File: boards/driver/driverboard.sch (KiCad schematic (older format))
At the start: 39 parts, among them J1 RJ45, J2 RJ45, P1 HE10-10, Q1 NDS355, Q2 NDS355, Q3 NDS355, Q4 NDS355, Q5 NDS355, Q6 NDS355, Q7 NDS355, Q8 NDS355, U1 74HC595, U2 TS2937

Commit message: Small update on driverboard
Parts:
- R10, R3, R4, R5, R6, R7, R8, R9: value 200 -> 220
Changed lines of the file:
@@
 Sheet 1 1
 Title ""
-Date "26 jan 2014"
+Date "15 apr 2014"
 Rev ""
 Comp ""
@@
 P 8950 6600
 F 0 "R10" V 9030 6600 40  0000 C CNN
-F 1 "200" V 8957 6601 40  0000 C CNN
+F 1 "220" V 8957 6601 40  0000 C CNN
 F 2 "~" V 8880 6600 30  0000 C CNN
 F 3 "~" H 8950 6600 30  0000 C CNN
@@
 P 8950 5850
 F 0 "R9" V 9030 5850 40  0000 C CNN
-F 1 "200" V 8957 5851 40  0000 C CNN
+F 1 "220" V 8957 5851 40  0000 C CNN
 F 2 "~" V 8880 5850 30  0000 C CNN
 F 3 "~" H 8950 5850 30  0000 C CNN
@@
 P 8950 5100
 F 0 "R8" V 9030 5100 40  0000 C CNN
-F 1 "200" V 8957 5101 40  0000 C CNN
+F 1 "220" V 8957 5101 40  0000 C CNN
 F 2 "~" V 8880 5100 30  0000 C CNN
 F 3 "~" H 8950 5100 30  0000 C CNN
@@
 P 8950 4350
 F 0 "R7" V 9030 4350 40  0000 C CNN
-F 1 "200" V 8957 4351 40  0000 C CNN
+F 1 "220" V 8957 4351 40  0000 C CNN
 F 2 "~" V 8880 4350 30  0000 C CNN
 F 3 "~" H 8950 4350 30  0000 C CNN
@@
 P 8950 3600
 F 0 "R6" V 9030 3600 40  0000 C CNN
-F 1 "200" V 8957 3601 40  0000 C CNN
+F 1 "220" V 8957 3601 40  0000 C CNN
 F 2 "~" V 8880 3600 30  0000 C CNN
 F 3 "~" H 8950 3600 30  0000 C CNN
@@
 P 8950 2850
 F 0 "R5" V 9030 2850 40  0000 C CNN
-F 1 "200" V 8957 2851 40  0000 C CNN
+F 1 "220" V 8957 2851 40  0000 C CNN
 F 2 "~" V 8880 2850 30  0000 C CNN
 F 3 "~" H 8950 2850 30  0000 C CNN
@@
 P 8950 2100
 F 0 "R4" V 9030 2100 40  0000 C CNN
-F 1 "200" V 8957 2101 40  0000 C CNN
+F 1 "220" V 8957 2101 40  0000 C CNN
 F 2 "~" V 8880 2100 30  0000 C CNN
 F 3 "~" H 8950 2100 30  0000 C CNN
@@
 P 8950 1350
 F 0 "R3" V 9030 1350 40  0000 C CNN
-F 1 "200" V 8957 1351 40  0000 C CNN
+F 1 "220" V 8957 1351 40  0000 C CNN
 F 2 "~" V 8880 1350 30  0000 C CNN
 F 3 "~" H 8950 1350 30  0000 C CNN

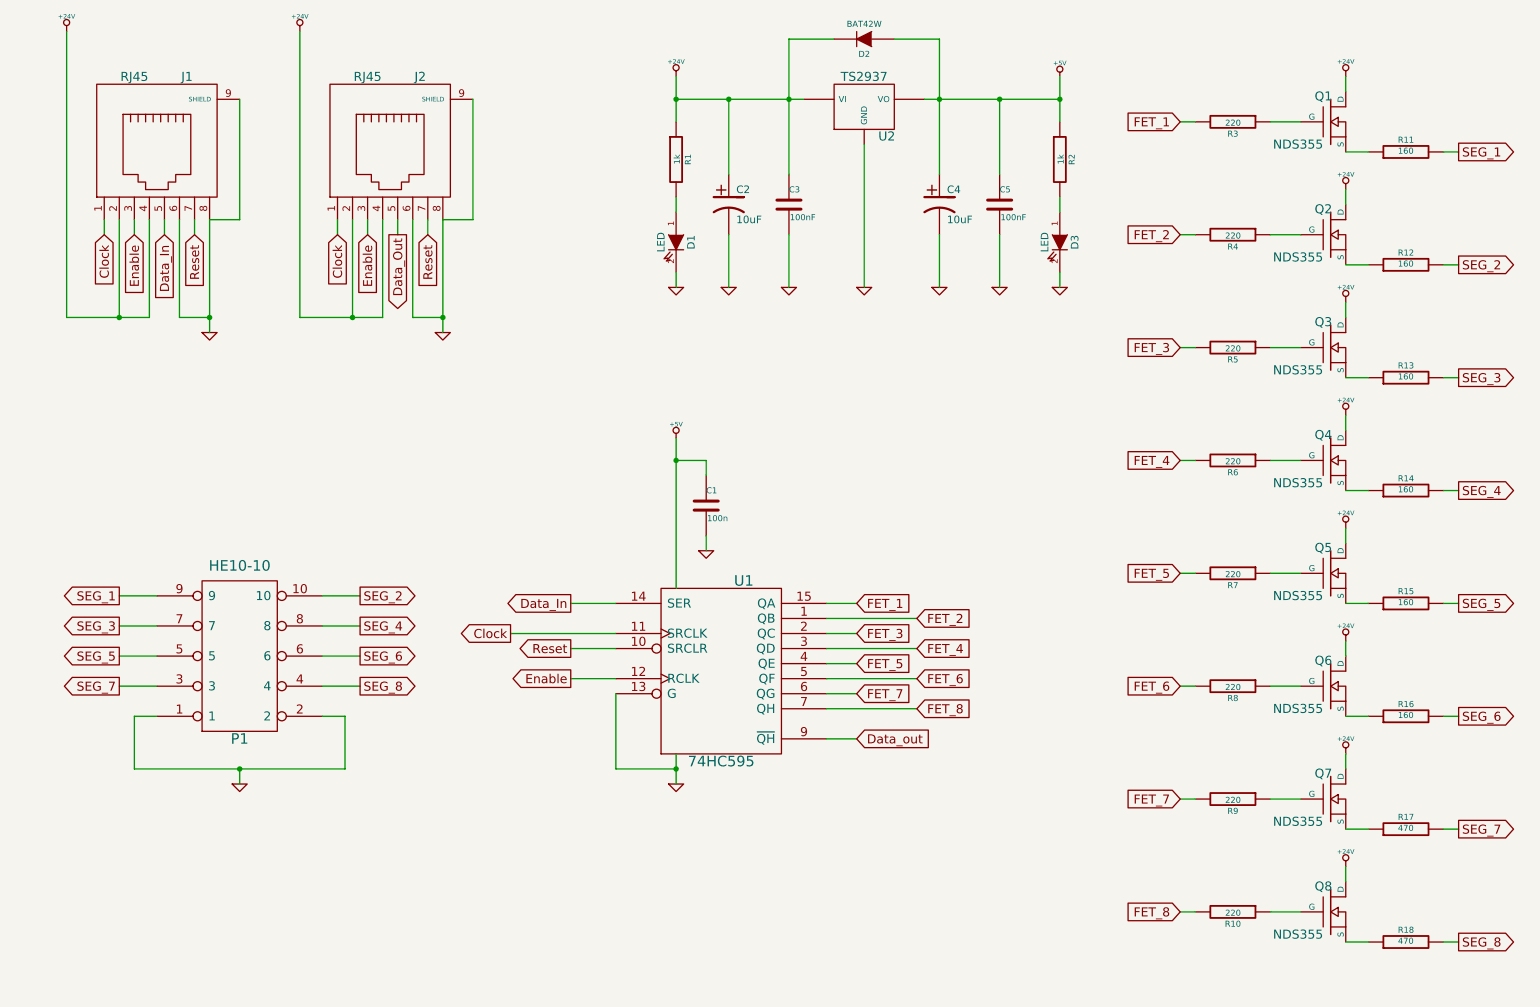
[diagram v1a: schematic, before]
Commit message: Started fixing schematics
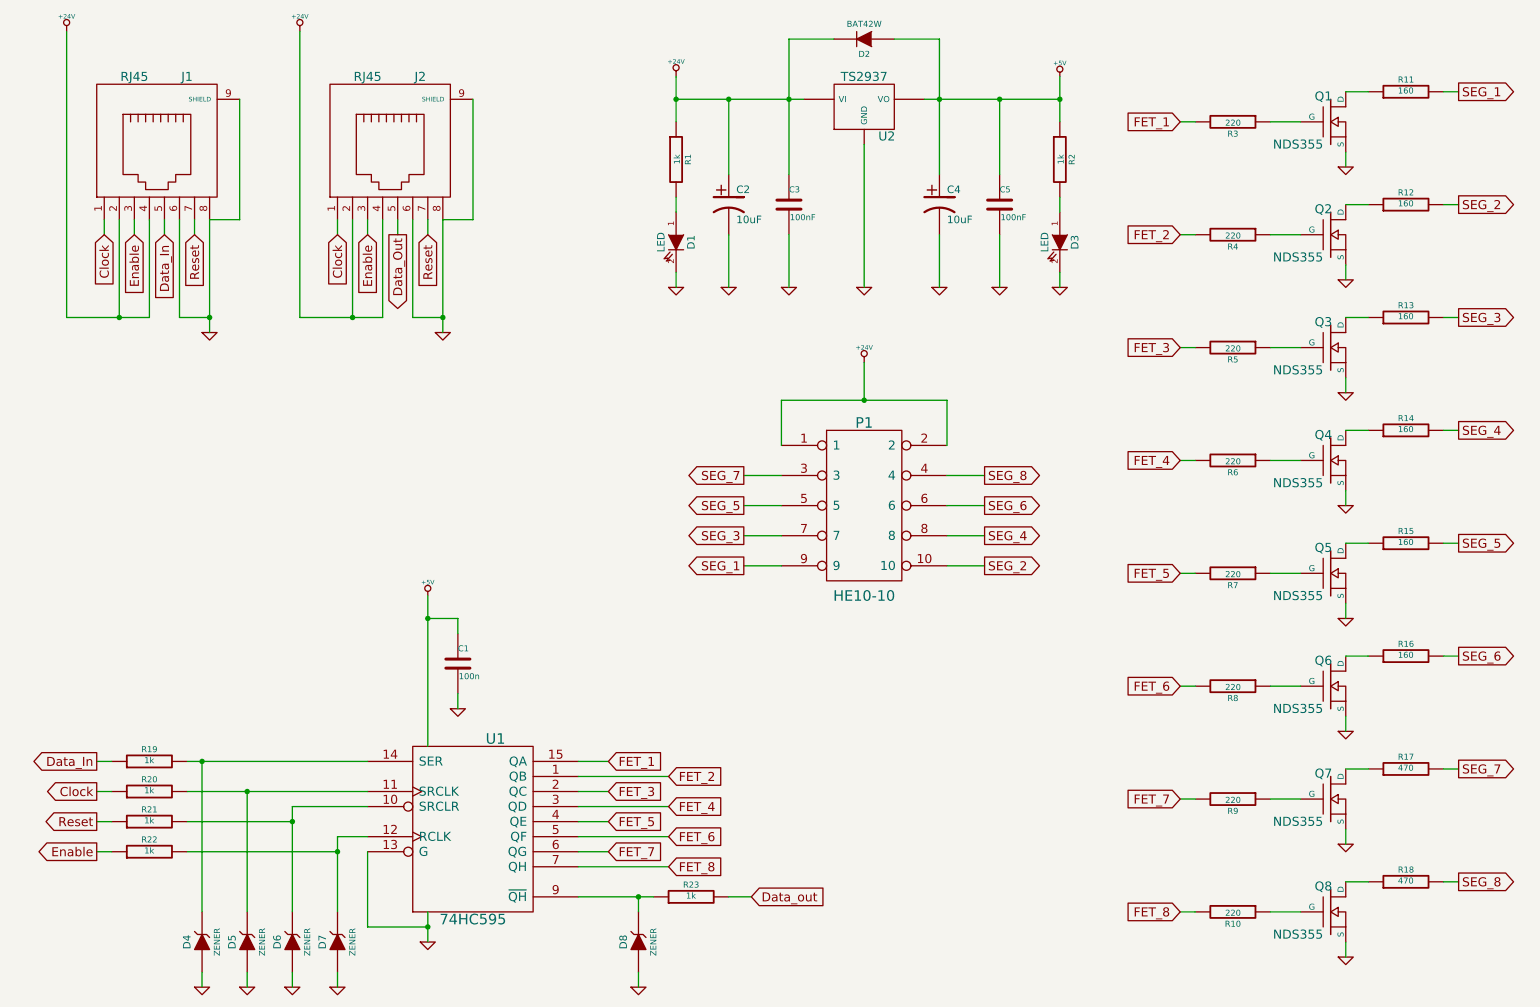
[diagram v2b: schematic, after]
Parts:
- added D4, D5, D6, D7, D8: ZENER, ~, symbol ZENER
- added R19, R20, R21, R22, R23: 1k, ~, symbol R
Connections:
- net +24V: now also P1.1, P1.2; no longer Q1.2 (D), Q2.2 (D), Q3.2 (D), Q4.2 (D), Q5.2 (D), Q6.2 (D), Q7.2 (D), Q8.2 (D)
- net Clock: now also R20.1; no longer U1.11 (SRCLK)
- net Data_In: now also R19.1; no longer U1.14 (SER)
- net Data_out: now also R23.2; no longer U1.9 (~QH)
- net Enable: now also R22.1; no longer U1.12 (RCLK)
- net GND: now also Q1.3 (S), Q2.3 (S), Q3.3 (S), Q4.3 (S), Q5.3 (S), Q6.3 (S), Q7.3 (S), Q8.3 (S), D4.1 (A), D5.1 (A), D6.1 (A), D7.1 (A), D8.1 (A); no longer P1.1, P1.2
- net Reset: now also R21.1; no longer U1.10 (SRCLR)
- net at R18.1: now also Q8.2 (D); no longer Q8.3 (S)
- net at R17.1: now also Q7.2 (D); no longer Q7.3 (S)
- net at R16.1: now also Q6.2 (D); no longer Q6.3 (S)
- net at R15.1: now also Q5.2 (D); no longer Q5.3 (S)
- net at R14.1: now also Q4.2 (D); no longer Q4.3 (S)
- net at R13.1: now also Q3.2 (D); no longer Q3.3 (S)
- net at R12.1: now also Q2.2 (D); no longer Q2.3 (S)
- net at R11.1: now also Q1.2 (D); no longer Q1.3 (S)
- new net: D6.2 (K), R21.2, U1.10 (SRCLR)
- new net: D5.2 (K), R20.2, U1.11 (SRCLK)
- new net: D7.2 (K), R22.2, U1.12 (RCLK)
- new net: D4.2 (K), R19.2, U1.14 (SER)
- new net: D8.2 (K), R23.1, U1.9 (~QH)
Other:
- moved on the sheet: C1, P1, R11, R12, R13, R14, R15, R16, R17, R18, U1

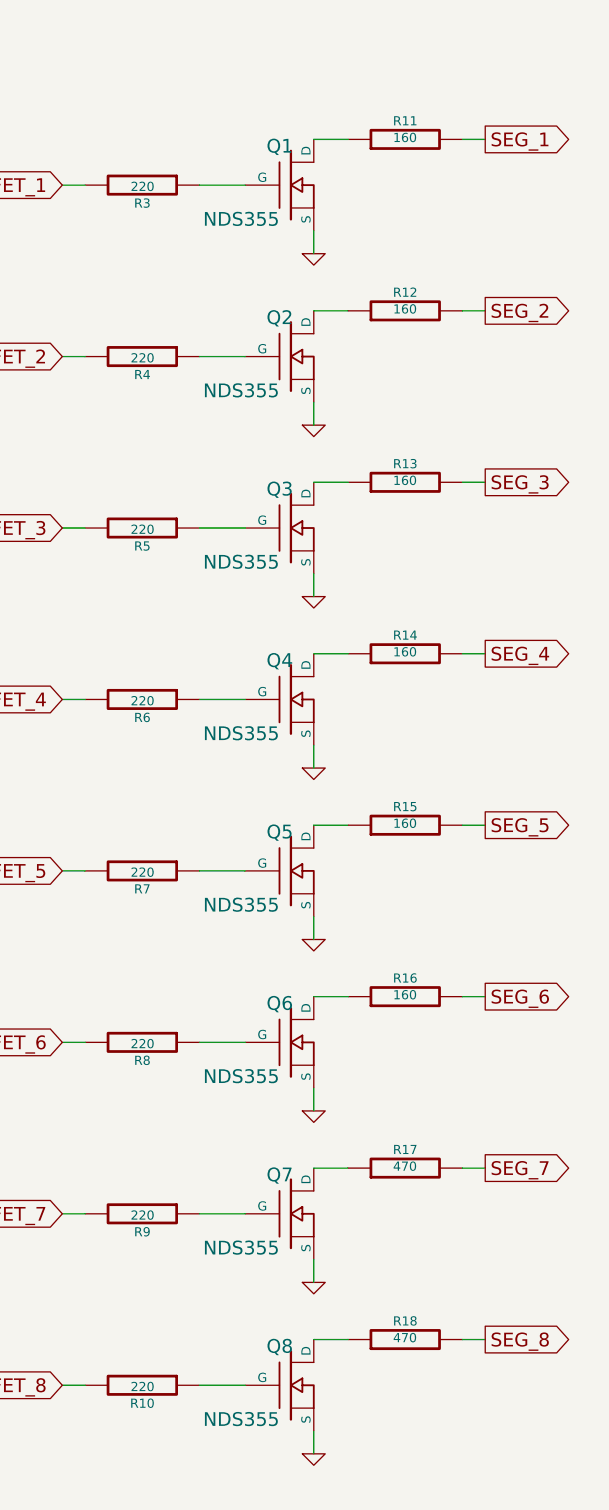
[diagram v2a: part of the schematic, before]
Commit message: Updated resistor values
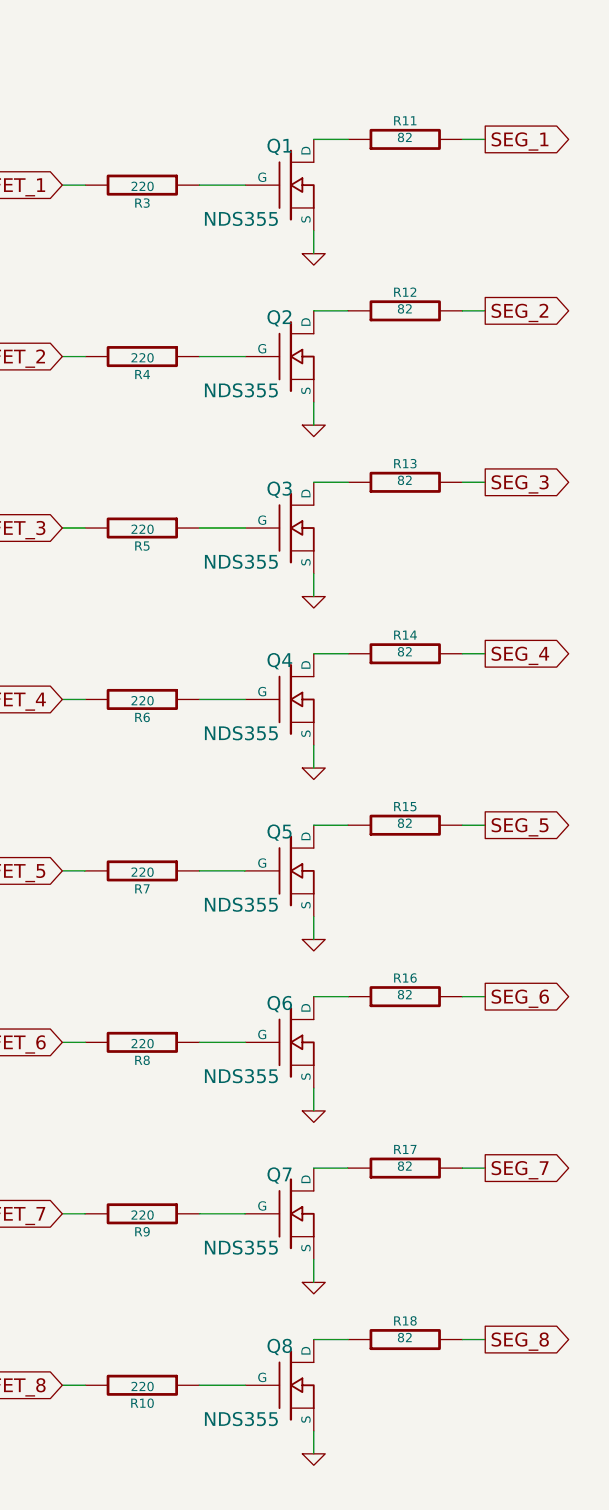
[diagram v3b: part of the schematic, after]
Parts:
- R11, R12, R13, R14, R15, R16: value 160 -> 82
- R17, R18: value 470 -> 82
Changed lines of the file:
@@
 Sheet 1 1
 Title ""
-Date "15 aug 2014"
+Date "21 nov 2014"
 Rev ""
 Comp ""
@@
 P 10100 6400
 F 0 "R18" V 10180 6400 40  0000 C CNN
-F 1 "470" V 10107 6401 40  0000 C CNN
+F 1 "82" V 10107 6401 40  0000 C CNN
 F 2 "~" V 10030 6400 30  0000 C CNN
 F 3 "~" H 10100 6400 30  0000 C CNN
@@
 P 10100 5650
 F 0 "R17" V 10180 5650 40  0000 C CNN
-F 1 "470" V 10107 5651 40  0000 C CNN
+F 1 "82" V 10107 5651 40  0000 C CNN
 F 2 "~" V 10030 5650 30  0000 C CNN
 F 3 "~" H 10100 5650 30  0000 C CNN
@@
 P 10100 4900
 F 0 "R16" V 10180 4900 40  0000 C CNN
-F 1 "160" V 10107 4901 40  0000 C CNN
+F 1 "82" V 10107 4901 40  0000 C CNN
 F 2 "~" V 10030 4900 30  0000 C CNN
 F 3 "~" H 10100 4900 30  0000 C CNN
@@
 P 10100 4150
 F 0 "R15" V 10180 4150 40  0000 C CNN
-F 1 "160" V 10107 4151 40  0000 C CNN
+F 1 "82" V 10107 4151 40  0000 C CNN
 F 2 "~" V 10030 4150 30  0000 C CNN
 F 3 "~" H 10100 4150 30  0000 C CNN
@@
 P 10100 3400
 F 0 "R14" V 10180 3400 40  0000 C CNN
-F 1 "160" V 10107 3401 40  0000 C CNN
+F 1 "82" V 10107 3401 40  0000 C CNN
 F 2 "~" V 10030 3400 30  0000 C CNN
 F 3 "~" H 10100 3400 30  0000 C CNN
@@
 P 10100 2650
 F 0 "R13" V 10180 2650 40  0000 C CNN
-F 1 "160" V 10107 2651 40  0000 C CNN
+F 1 "82" V 10107 2651 40  0000 C CNN
 F 2 "~" V 10030 2650 30  0000 C CNN
 F 3 "~" H 10100 2650 30  0000 C CNN
@@
 P 10100 1900
 F 0 "R12" V 10180 1900 40  0000 C CNN
-F 1 "160" V 10107 1901 40  0000 C CNN
+F 1 "82" V 10107 1901 40  0000 C CNN
 F 2 "~" V 10030 1900 30  0000 C CNN
 F 3 "~" H 10100 1900 30  0000 C CNN
@@
 P 10100 1150
 F 0 "R11" V 10180 1150 40  0000 C CNN
-F 1 "160" V 10107 1151 40  0000 C CNN
+F 1 "82" V 10107 1151 40  0000 C CNN
 F 2 "~" V 10030 1150 30  0000 C CNN
 F 3 "~" H 10100 1150 30  0000 C CNN
